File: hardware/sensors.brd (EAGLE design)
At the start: 80 x 80 mm, 30 parts, among them U1 DS18B20, U2 DS18B20, U3 DS18B20

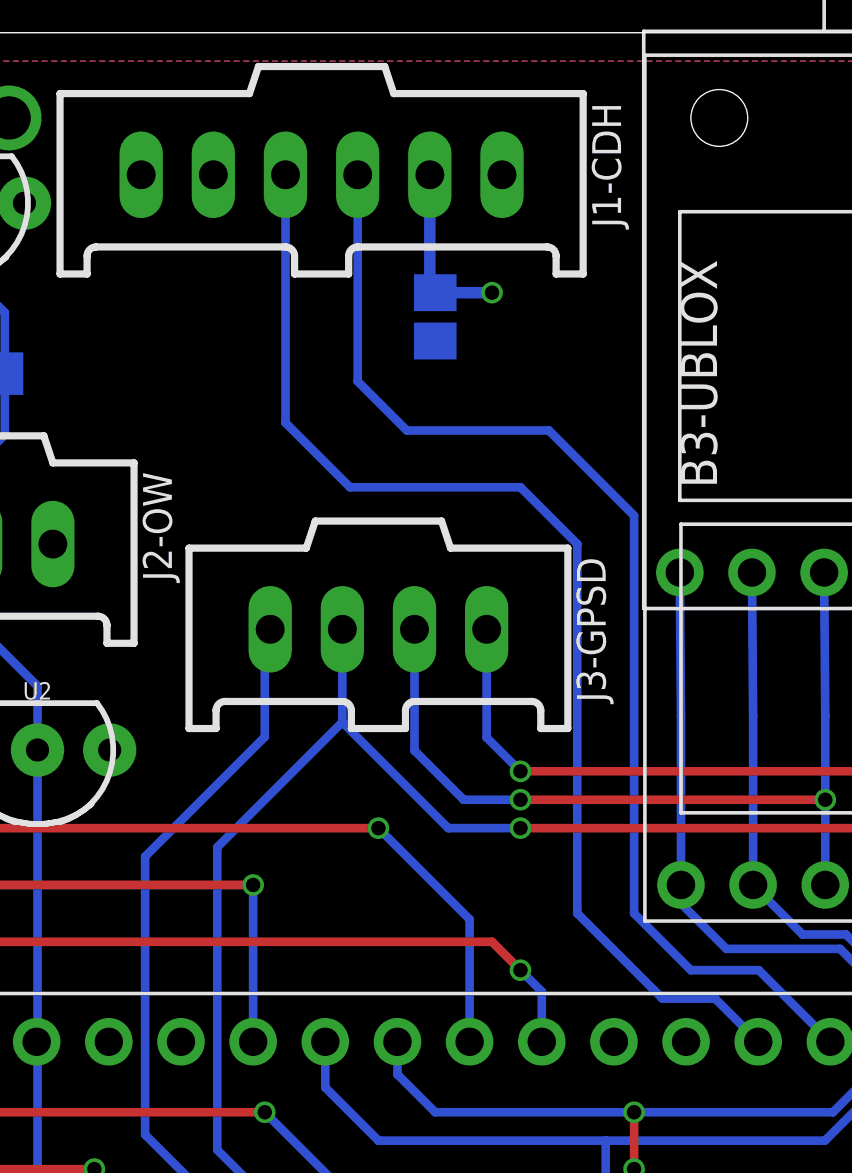
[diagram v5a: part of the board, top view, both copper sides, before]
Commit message: Move debug connector
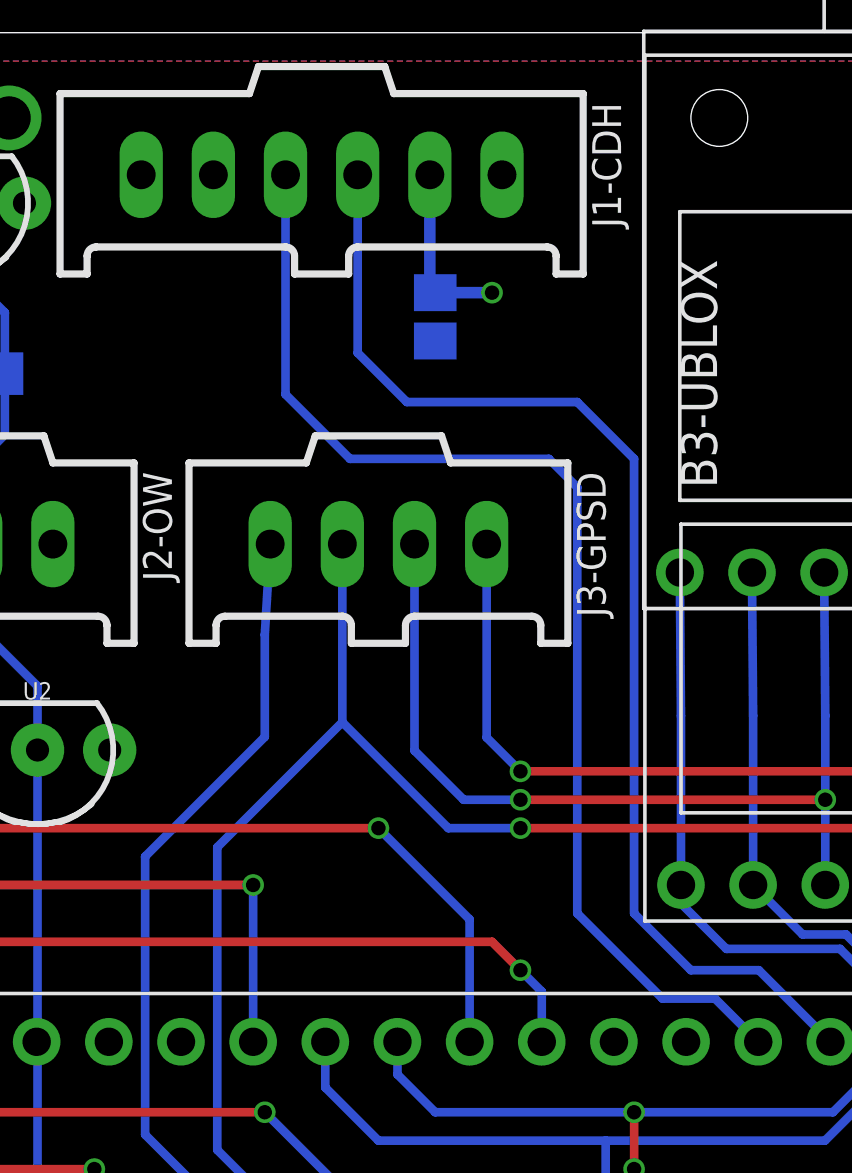
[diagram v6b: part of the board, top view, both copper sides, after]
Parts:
- moved J3-GPSD 3.00 mm to (48.0, 62.0)
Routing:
- net GPS-TX: track 30.4 -> 33.4 mm
- net GPS-TP: track 75.7 -> 78.7 mm
- net GPS-RX: track 29.8 -> 32.8 mm
- net DBG-TX: track 33.2 -> 36.1 mm
- net CDH-TX: track 41.7 -> 42.3 mm
- net CDH-RX: track 42.0 -> 42.6 mm
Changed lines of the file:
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@@
 <element name="B4-OPENLOG" library="Frcy" package="SPARKFUN-OPENLOG" value="" x="65" y="16" rot="R180"/>
 <element name="J2-OW" library="con-molex-c-grid" package="90136-1?03" value="" x="34" y="62" rot="R180"/>
-<element name="J3-GPSD" library="con-molex-c-grid" package="90136-1?04" value="" x="48" y="59" rot="R180"/>
+<element name="J3-GPSD" library="con-molex-c-grid" package="90136-1?04" value="" x="48" y="62" rot="R180"/>
 <element name="J1-CDH" library="con-molex-c-grid" package="90136-1?06" value="" x="46" y="75" rot="R180"/>
 <element name="R1" library="rcl" library_urn="urn:adsk.eagle:library:334" package="R2012" package3d_urn="urn:adsk.eagle:package:23543/2" value="4.7k" x="34" y="68" rot="MR0">
@@
 <wire x1="61.39" y1="47" x2="59" y2="47" width="0.3048" layer="16"/>
 <wire x1="59" y1="47" x2="57" y2="49" width="0.3048" layer="16"/>
-<wire x1="57" y1="49" x2="57" y2="63" width="0.3048" layer="16"/>
-<wire x1="57" y1="63" x2="54" y2="66" width="0.3048" layer="16"/>
-<wire x1="49" y1="66" x2="47.27" y2="67.73" width="0.3048" layer="16"/>
-<wire x1="47.27" y1="67.73" x2="47.27" y2="75" width="0.3048" layer="16"/>
-<wire x1="54" y1="66" x2="49" y2="66" width="0.3048" layer="16"/>
+<wire x1="49" y1="67" x2="47.27" y2="68.73" width="0.3048" layer="16"/>
+<wire x1="47.27" y1="68.73" x2="47.27" y2="75" width="0.3048" layer="16"/>
+<wire x1="57" y1="65" x2="55" y2="67" width="0.3048" layer="16"/>
+<wire x1="57" y1="49" x2="57" y2="65" width="0.3048" layer="16"/>
+<wire x1="55" y1="67" x2="49" y2="67" width="0.3048" layer="16"/>
 </signal>
 <signal name="CDH-RX">
@@
 <wire x1="61.37" y1="44.48" x2="59.85" y2="46" width="0.3048" layer="16"/>
 <wire x1="58" y1="46" x2="59.85" y2="46" width="0.3048" layer="16"/>
-<wire x1="44.73" y1="75" x2="44.73" y2="66.27" width="0.3048" layer="16"/>
-<wire x1="44.73" y1="66.27" x2="47" y2="64" width="0.3048" layer="16"/>
-<wire x1="47" y1="64" x2="53" y2="64" width="0.3048" layer="16"/>
-<wire x1="53" y1="64" x2="55" y2="62" width="0.3048" layer="16"/>
-<wire x1="55" y1="62" x2="55" y2="49" width="0.3048" layer="16"/>
-<wire x1="55" y1="49" x2="58" y2="46" width="0.3048" layer="16"/>
+<wire x1="58" y1="46" x2="55" y2="49" width="0.3048" layer="16"/>
+<wire x1="55" y1="64" x2="54" y2="65" width="0.3048" layer="16"/>
+<wire x1="54" y1="65" x2="47" y2="65" width="0.3048" layer="16"/>
+<wire x1="47" y1="65" x2="44.73" y2="67.27" width="0.3048" layer="16"/>
+<wire x1="44.73" y1="67.27" x2="44.73" y2="75" width="0.3048" layer="16"/>
+<wire x1="55" y1="49" x2="55" y2="64" width="0.3048" layer="16"/>
 </signal>
 <signal name="SPI-MOSI">
@@
 <wire x1="43.59" y1="37.41" x2="39.788" y2="41.212" width="0.3048" layer="16"/>
 <wire x1="39.788" y1="51" x2="39.788" y2="41.212" width="0.3048" layer="16"/>
-<wire x1="44.19" y1="59" x2="44" y2="58.81" width="0.3048" layer="16"/>
+<wire x1="44.19" y1="62" x2="44" y2="58.81" width="0.3048" layer="16"/>
 <wire x1="44" y1="55.212" x2="39.788" y2="51" width="0.3048" layer="16"/>
 <wire x1="44" y1="58.81" x2="44" y2="55.212" width="0.3048" layer="16"/>
@@
 <wire x1="53" y1="53" x2="51" y2="53" width="0.3048" layer="16"/>
 <wire x1="51" y1="53" x2="49.27" y2="54.73" width="0.3048" layer="16"/>
-<wire x1="49.27" y1="54.73" x2="49.27" y2="59" width="0.3048" layer="16"/>
+<wire x1="49.27" y1="54.73" x2="49.27" y2="62" width="0.3048" layer="16"/>
 </signal>
 <signal name="GPS-RX">
@@
 <via x="53" y="54" extent="1-16" drill="0.508"/>
 <wire x1="53" y1="54" x2="51.81" y2="55.19" width="0.3048" layer="16"/>
-<wire x1="51.81" y1="55.19" x2="51.81" y2="59" width="0.3048" layer="16"/>
+<wire x1="51.81" y1="55.19" x2="51.81" y2="62" width="0.3048" layer="16"/>
 <contactref element="B7-UBLOXE" pad="RXD"/>
 <wire x1="66.27" y1="50" x2="66.27" y2="54" width="0.3048" layer="16"/>
@@
 <wire x1="46.13" y1="29.24" x2="46.13" y2="36.87" width="0.3048" layer="16"/>
 <wire x1="46.13" y1="36.87" x2="42.328" y2="40.672" width="0.3048" layer="16"/>
-<wire x1="46.73" y1="55.73" x2="46.73" y2="59" width="0.3048" layer="16"/>
+<wire x1="46.73" y1="55.73" x2="46.73" y2="62" width="0.3048" layer="16"/>
 <wire x1="42.328" y1="40.672" x2="42.328" y2="51.328" width="0.3048" layer="16"/>
 <wire x1="42.328" y1="51.328" x2="46.73" y2="55.73" width="0.3048" layer="16"/>

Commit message: Move external GPS chip
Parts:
- moved B7-UBLOXE 8.00 mm to (67.5, 53.0)
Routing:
- net GPS-TP: track 78.7 -> 64.0 mm
- net GPS-SDA: track 46.8 -> 38.8 mm
- net GPS-TX: track 33.4 -> 26.4 mm
- net GPS-SCL: track 51.8 -> 44.9 mm
- net GPS-RX: track 32.8 -> 26.4 mm
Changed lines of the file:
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@@
 </element>
 <element name="B6-BLE" library="Frcy" package="HUAMAO-HM-11" value="" x="57" y="14" rot="R270"/>
-<element name="B7-UBLOXE" library="Frcy" package="UPUTRONICS-UBLOX-M8Q" value="" x="67.5" y="61"/>
+<element name="B7-UBLOXE" library="Frcy" package="UPUTRONICS-UBLOX-M8Q" value="" x="67.5" y="53"/>
 </elements>
 <signals>
@@
 <wire x1="60.85" y1="39" x2="63" y2="39" width="0.3048" layer="16"/>
 <wire x1="60.85" y1="36" x2="63" y2="36" width="0.3048" layer="16"/>
-<wire x1="71.35" y1="50" x2="71.35" y2="48.35" width="0.3048" layer="16"/>
-<wire x1="71.35" y1="48.35" x2="71" y2="48" width="0.3048" layer="16"/>
-<via x="71" y="48" extent="1-16" drill="0.508"/>
-<wire x1="76.39" y1="61" x2="76.39" y2="59.39" width="0.3048" layer="16"/>
-<wire x1="76.39" y1="59.39" x2="76" y2="59" width="0.3048" layer="16"/>
-<via x="76" y="59" extent="1-16" drill="0.508"/>
+<wire x1="76.39" y1="53" x2="76.39" y2="51" width="0.3048" layer="16"/>
+<via x="76.39" y="51" extent="1-16" drill="0.508"/>
+<wire x1="71.35" y1="50" x2="71.35" y2="48" width="0.3048" layer="16"/>
+<via x="71.35" y="48" extent="1-16" drill="0.508"/>
 </signal>
 <signal name="GND">
@@
 <wire x1="57" y1="40" x2="58" y2="39" width="0.3048" layer="16"/>
 <wire x1="58" y1="39" x2="59.15" y2="39" width="0.3048" layer="16"/>
-<wire x1="58.65" y1="50" x2="58.65" y2="55.96" width="0.3048" layer="16"/>
-<wire x1="58.65" y1="55.96" x2="58.61" y2="61" width="0.3048" layer="16"/>
+<wire x1="58.65" y1="50" x2="58.65" y2="52.96" width="0.3048" layer="16"/>
+<wire x1="58.65" y1="52.96" x2="58.61" y2="53" width="0.3048" layer="16"/>
 </signal>
 <signal name="GPS-SCL">
@@
 <contactref element="R5" pad="2"/>
 <wire x1="46.13" y1="44.48" x2="46.13" y2="42.87" width="0.3048" layer="16"/>
-<wire x1="66.508" y1="46.210425" x2="64.460425" y2="48.258" width="0.3048" layer="16"/>
+<wire x1="64.460425" y1="48.258" x2="66.508" y2="46.210425" width="0.3048" layer="16"/>
 <wire x1="66.508" y1="43.789575" x2="66.508" y2="46.210425" width="0.3048" layer="16"/>
-<wire x1="62.932" y1="48.258" x2="61.19" y2="50" width="0.3048" layer="16"/>
-<wire x1="64.460425" y1="48.258" x2="62.932" y2="48.258" width="0.3048" layer="16"/>
 <contactref element="B7-UBLOXE" pad="SCL"/>
 <wire x1="46.13" y1="42.87" x2="48" y2="41" width="0.3048" layer="16"/>
-<wire x1="48" y1="41" x2="56" y2="41" width="0.3048" layer="16"/>
-<wire x1="56" y1="41" x2="63.718425" y2="41" width="0.3048" layer="16"/>
+<wire x1="48" y1="41" x2="55" y2="41" width="0.3048" layer="16"/>
+<wire x1="55" y1="41" x2="63.718425" y2="41" width="0.3048" layer="16"/>
 <wire x1="63.718425" y1="41" x2="66.508" y2="43.789575" width="0.3048" layer="16"/>
-<wire x1="56" y1="41" x2="56" y2="37" width="0.3048" layer="16"/>
-<wire x1="56" y1="37" x2="57" y2="36" width="0.3048" layer="16"/>
-<wire x1="57" y1="36" x2="59.15" y2="36" width="0.3048" layer="16"/>
-<wire x1="61.19" y1="50" x2="61.19" y2="55.96" width="0.3048" layer="16"/>
-<wire x1="61.19" y1="55.96" x2="61.15" y2="61" width="0.3048" layer="16"/>
+<wire x1="59.15" y1="36" x2="57" y2="36" width="0.3048" layer="16"/>
+<wire x1="61.19" y1="50" x2="61.19" y2="48.81" width="0.3048" layer="16"/>
+<wire x1="61.19" y1="48.81" x2="61.742" y2="48.258" width="0.3048" layer="16"/>
+<wire x1="61.742" y1="48.258" x2="64.460425" y2="48.258" width="0.3048" layer="16"/>
+<wire x1="61.19" y1="50" x2="61.19" y2="52.96" width="0.3048" layer="16"/>
+<wire x1="61.19" y1="52.96" x2="61.15" y2="53" width="0.3048" layer="16"/>
+<wire x1="55" y1="38" x2="55" y2="41" width="0.3048" layer="16"/>
+<wire x1="57" y1="36" x2="55" y2="38" width="0.3048" layer="16"/>
 </signal>
 <signal name="LOG-TX">
@@
 <wire x1="43.59" y1="29.24" x2="43.59" y2="37.41" width="0.3048" layer="16"/>
 <wire x1="43.59" y1="37.41" x2="39.788" y2="41.212" width="0.3048" layer="16"/>
-<wire x1="39.788" y1="51" x2="39.788" y2="41.212" width="0.3048" layer="16"/>
-<wire x1="44.19" y1="62" x2="44" y2="58.81" width="0.3048" layer="16"/>
-<wire x1="44" y1="55.212" x2="39.788" y2="51" width="0.3048" layer="16"/>
-<wire x1="44" y1="58.81" x2="44" y2="55.212" width="0.3048" layer="16"/>
+<wire x1="39.788" y1="41.212" x2="39.788" y2="51" width="0.3048" layer="16"/>
+<wire x1="39.788" y1="51" x2="44.19" y2="55.402" width="0.3048" layer="16"/>
+<wire x1="44.19" y1="55.402" x2="44.19" y2="62" width="0.3048" layer="16"/>
 </signal>
 <signal name="VIN">
@@
 <contactref element="B3-UBLOX" pad="TXD"/>
 <contactref element="J3-GPSD" pad="2"/>
-<via x="53" y="53" extent="1-16" drill="0.508"/>
 <contactref element="B7-UBLOXE" pad="TXD"/>
-<wire x1="63.73" y1="50" x2="63.73" y2="53" width="0.3048" layer="16"/>
-<wire x1="63.73" y1="53" x2="63.73" y2="55.96" width="0.3048" layer="16"/>
-<wire x1="63.73" y1="55.96" x2="63.69" y2="61" width="0.3048" layer="16"/>
-<via x="63.73" y="53" extent="1-16" drill="0.508"/>
-<wire x1="53" y1="53" x2="63.73" y2="53" width="0.3048" layer="1"/>
-<wire x1="53" y1="53" x2="51" y2="53" width="0.3048" layer="16"/>
-<wire x1="51" y1="53" x2="49.27" y2="54.73" width="0.3048" layer="16"/>
-<wire x1="49.27" y1="54.73" x2="49.27" y2="62" width="0.3048" layer="16"/>
+<wire x1="49.27" y1="62" x2="49.27" y2="59" width="0.3048" layer="16"/>
+<wire x1="63.73" y1="50" x2="63.73" y2="52.96" width="0.3048" layer="16"/>
+<wire x1="63.73" y1="52.96" x2="63.69" y2="53" width="0.3048" layer="16"/>
+<wire x1="63.69" y1="53" x2="63.69" y2="59" width="0.3048" layer="16"/>
+<via x="63.69" y="59" extent="1-16" drill="0.508"/>
+<wire x1="63.69" y1="59" x2="49.27" y2="59" width="0.3048" layer="1"/>
+<via x="49.27" y="59" extent="1-16" drill="0.508"/>
 </signal>
 <signal name="GPS-RX">
 <contactref element="B3-UBLOX" pad="RXD"/>
 <contactref element="J3-GPSD" pad="1"/>
-<via x="53" y="54" extent="1-16" drill="0.508"/>
-<wire x1="53" y1="54" x2="51.81" y2="55.19" width="0.3048" layer="16"/>
-<wire x1="51.81" y1="55.19" x2="51.81" y2="62" width="0.3048" layer="16"/>
 <contactref element="B7-UBLOXE" pad="RXD"/>
-<wire x1="66.27" y1="50" x2="66.27" y2="54" width="0.3048" layer="16"/>
-<wire x1="66.27" y1="54" x2="66.27" y2="55.96" width="0.3048" layer="16"/>
-<wire x1="66.27" y1="55.96" x2="66.23" y2="61" width="0.3048" layer="16"/>
-<via x="66.27" y="54" extent="1-16" drill="0.508"/>
-<wire x1="53" y1="54" x2="66.27" y2="54" width="0.3048" layer="1"/>
+<wire x1="51.81" y1="62" x2="51.81" y2="57" width="0.3048" layer="16"/>
+<wire x1="66.27" y1="50" x2="66.27" y2="52.96" width="0.3048" layer="16"/>
+<wire x1="66.27" y1="52.96" x2="66.23" y2="53" width="0.3048" layer="16"/>
+<wire x1="66.23" y1="53" x2="66.23" y2="57" width="0.3048" layer="16"/>
+<via x="66.23" y="57" extent="1-16" drill="0.508"/>
+<wire x1="66.23" y1="57" x2="51.81" y2="57" width="0.3048" layer="1"/>
+<via x="51.81" y="57" extent="1-16" drill="0.508"/>
 </signal>
 <signal name="SPI-CS-SUN">
@@
 <wire x1="46.13" y1="29.24" x2="46.13" y2="36.87" width="0.3048" layer="16"/>
 <wire x1="46.13" y1="36.87" x2="42.328" y2="40.672" width="0.3048" layer="16"/>
-<wire x1="46.73" y1="55.73" x2="46.73" y2="62" width="0.3048" layer="16"/>
-<wire x1="42.328" y1="40.672" x2="42.328" y2="51.328" width="0.3048" layer="16"/>
-<wire x1="42.328" y1="51.328" x2="46.73" y2="55.73" width="0.3048" layer="16"/>
-<wire x1="46.73" y1="55.73" x2="50.46" y2="52" width="0.3048" layer="16"/>
-<wire x1="50.46" y1="52" x2="53" y2="52" width="0.3048" layer="16"/>
-<via x="53" y="52" extent="1-16" drill="0.508"/>
-<via x="68" y="52" extent="1-16" drill="0.508"/>
-<wire x1="53" y1="52" x2="68" y2="52" width="0.3048" layer="1"/>
-<wire x1="68" y1="52" x2="68.77" y2="52.77" width="0.3048" layer="16"/>
-<wire x1="68.77" y1="52.77" x2="68.77" y2="61" width="0.3048" layer="16"/>
-<wire x1="68" y1="52" x2="71.31" y2="55.31" width="0.3048" layer="16"/>
-<wire x1="71.31" y1="55.31" x2="71.31" y2="61" width="0.3048" layer="16"/>
+<wire x1="42.328" y1="40.672" x2="42.328" y2="50.598" width="0.3048" layer="16"/>
+<wire x1="68.77" y1="53" x2="68.77" y2="55" width="0.3048" layer="16"/>
+<wire x1="46.73" y1="62" x2="46.73" y2="55" width="0.3048" layer="16"/>
+<via x="68.77" y="55" extent="1-16" drill="0.508"/>
+<wire x1="68.77" y1="55" x2="46.73" y2="55" width="0.3048" layer="1"/>
+<via x="46.73" y="55" extent="1-16" drill="0.508"/>
+<wire x1="46.73" y1="55" x2="42.328" y2="50.598" width="0.3048" layer="16"/>
+<wire x1="68.77" y1="55" x2="70" y2="55" width="0.3048" layer="16"/>
+<wire x1="70" y1="55" x2="71.31" y2="53.69" width="0.3048" layer="16"/>
+<wire x1="71.31" y1="53.69" x2="71.31" y2="53" width="0.3048" layer="16"/>
 </signal>
 </signals>
